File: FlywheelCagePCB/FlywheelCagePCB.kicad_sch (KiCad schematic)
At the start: 10 parts, among them J1 Conn_01x05, J2 Conn_01x05, Q1 SFH320, U1 QRE1113GR, U2 SN74LVC2G14DBV, U3 SPX3819M5-L-3-3

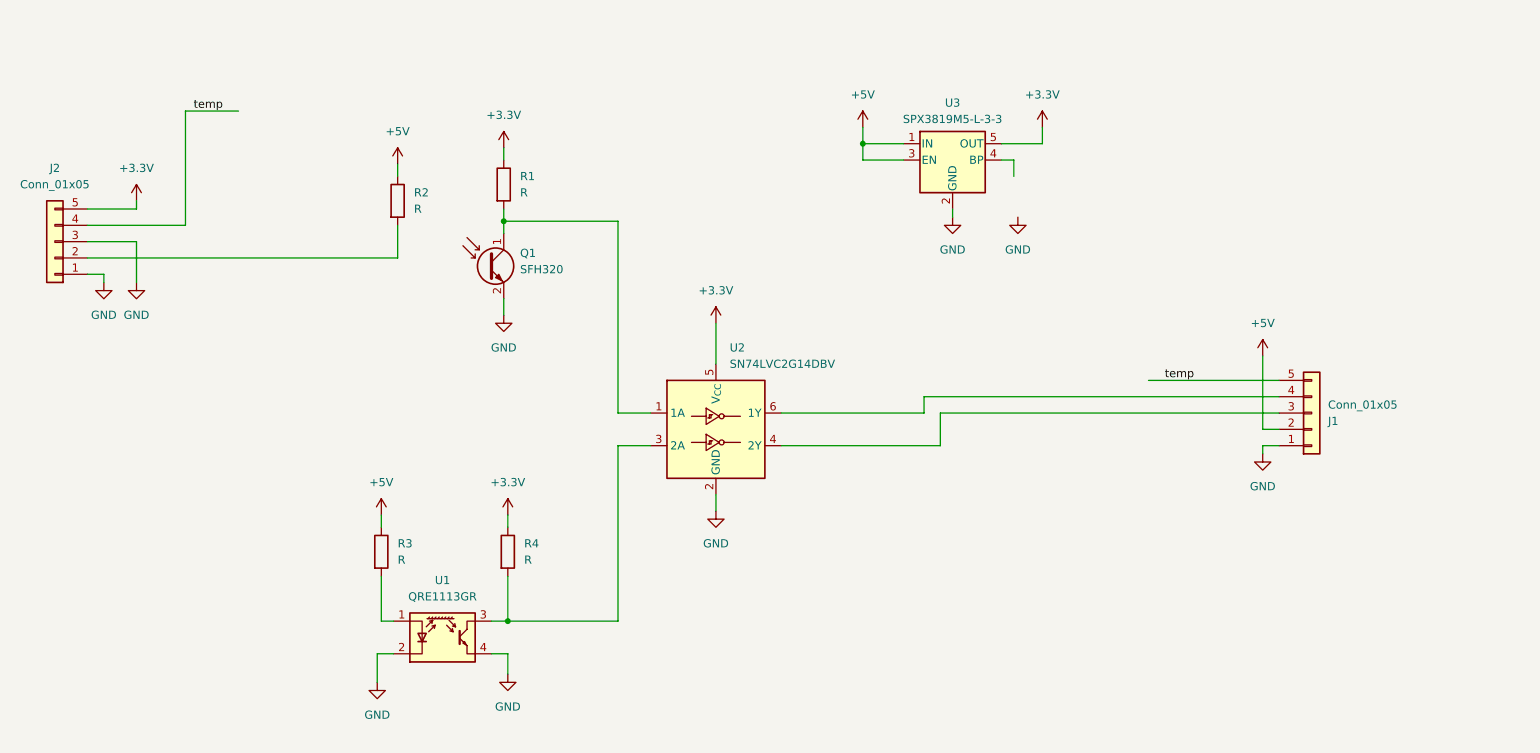
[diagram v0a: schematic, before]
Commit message: added resistors to flywheel pcb
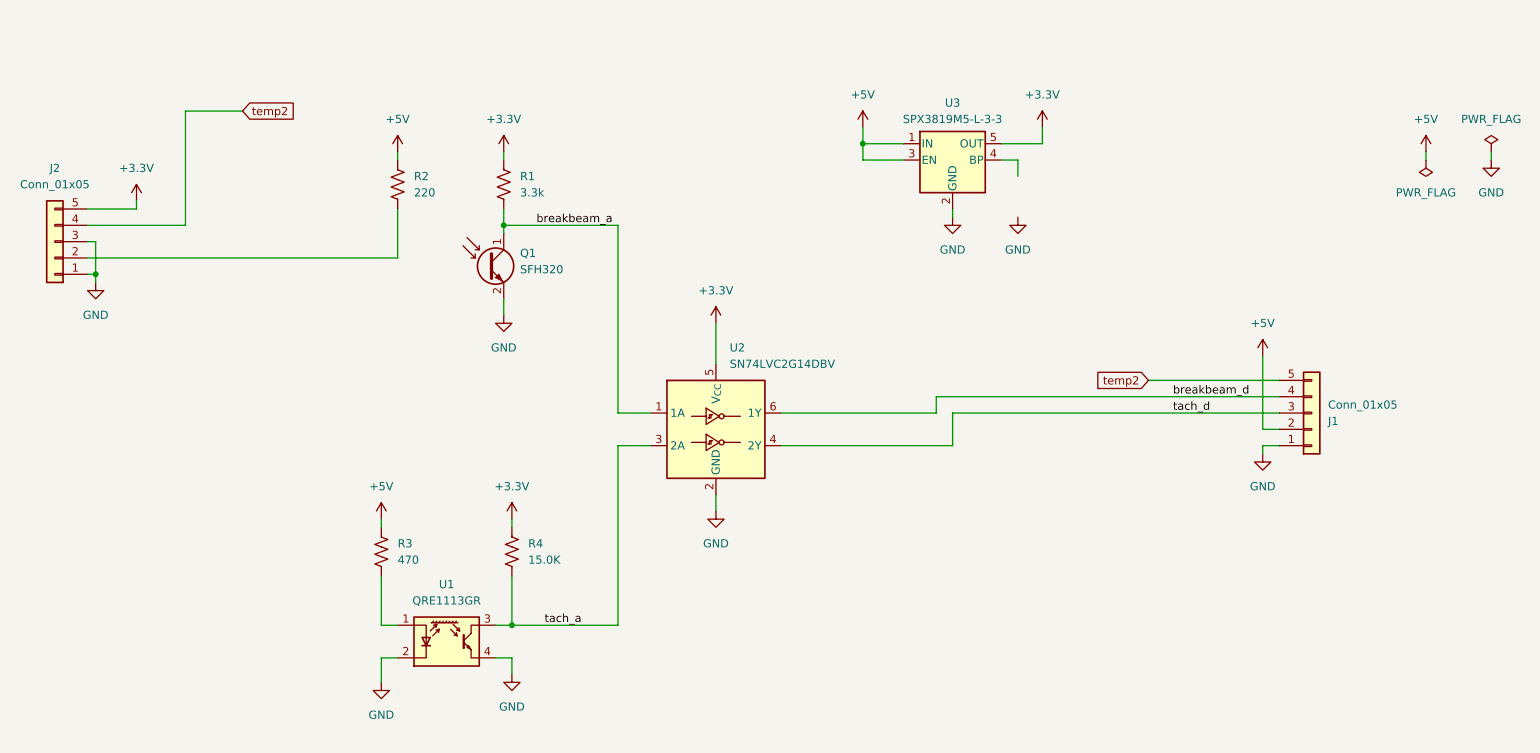
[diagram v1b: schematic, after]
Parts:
- removed R1, R2, R3, R4: R, symbol Device:R
- added R1: 3.3k, Resistor_SMD:R_0603_1608Metric, symbol Passives:R_3.3k_0603
- added R2: 220, Resistor_SMD:R_0603_1608Metric, symbol Passives:R_220_0603
- added R3: 470, Resistor_SMD:R_0603_1608Metric, symbol Passives:R_470_0603
- added R4: 15.0K, Resistor_SMD:R_0603_1608Metric, symbol Passives:R_15.0K_0603
- U2: PartNumber (none) -> 1727-6088-1-ND
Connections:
- net +3.3V: now also R1.1, R4.1
- net +5V: now also R2.1, R3.1
- net breakbeam_a: now reaches Q1.1 (C), U2.1 (1A)
- net breakbeam_a: now also R1.2
- net at U1.1 (A): now also R3.2
- net tach_a: now reaches U1.3, U2.3 (2A)
- net tach_a: now also R4.2
- net at J2.2 (Pin_2): now also R2.2
- net tach_d: now reaches J1.3 (Pin_3), U2.4 (2Y)
- net breakbeam_d: now reaches J1.4 (Pin_4), U2.6 (1Y)
- net temp renamed temp2
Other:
- moved on the sheet: U1

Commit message: moved PCB components a bit
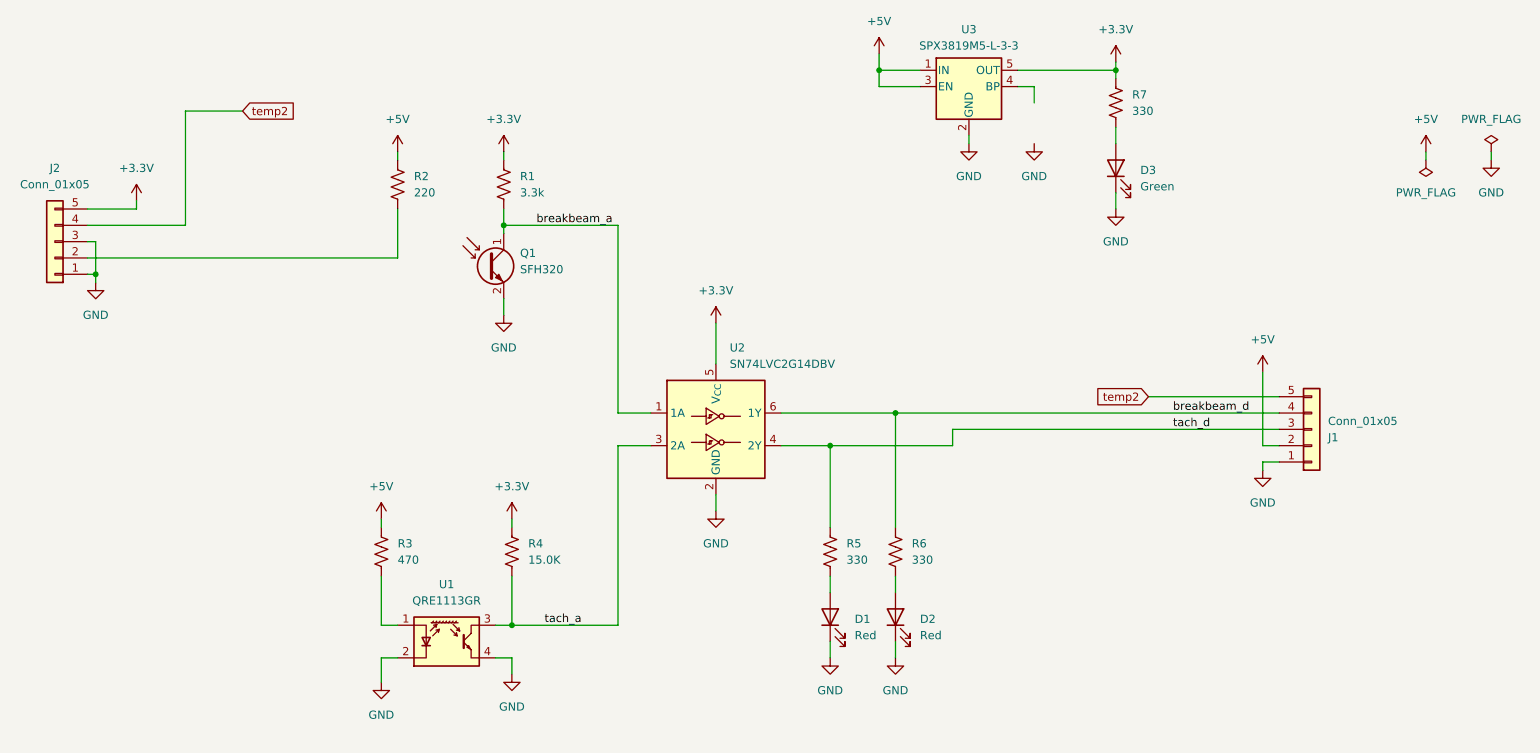
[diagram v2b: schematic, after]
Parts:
- added D1, D2: Red, symbol Passives:LED_RED_0603
- added D3: Green, LED_SMD:LED_0603_1608Metric, symbol Passives:LED_GREEN_0603
- added R5, R6, R7: 330, Resistor_SMD:R_0603_1608Metric, symbol Passives:R_330_0603
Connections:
- net +3.3V: now also R7.1
- net GND: now also D1.1 (K), D2.1 (K), D3.1 (K)
- net breakbeam_d: now also R6.1
- net tach_d: now also R5.1
- new net: D2.2 (A), R6.2
- new net: D1.2 (A), R5.2
- new net: D3.2 (A), R7.2
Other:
- moved on the sheet: J1, U3

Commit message: Added 3d models for JST ZH connectors.  Made 3d Step output
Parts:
- removed Q1: SFH320, LED_SMD:LED_PLCC-2_3.4x3.0mm_KA, symbol Sensor_Optical:SFH320
- added D4: SFH_320-4-Z, McLibrary:PHODET_SFH_320-4-Z, symbol Passives:SFH_320-4-Z
- D1, D2: footprint (none) -> LED_SMD:LED_0603_1608Metric
- J1, J2: footprint Connector_JST:JST_ZH_S5B-ZR-SM4A-TF_1x05-1MP_P1.50mm_Horizontal -> McLibrary:JST_ZH_B5B-ZR_1x05_P1.50mm_Horizontal; symbol Connector_Generic:Conn_01x05 -> Passives:Conn_JST_ZH_S5B_Horizontal_01x05
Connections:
- net GND: now also D4.E
- net breakbeam_a: now also D4.C
- net breakbeam_led_ind: now reaches D2.2 (A), R6.2
- net breakbeam_led: now reaches J2.2 (Pin_2), R2.2
- net tach_led: now reaches R3.2, U1.1 (A)
- net tach_led_ind: now reaches D1.2 (A), R5.2
- net power_led_ind: now reaches D3.2 (A), R7.2
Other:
- moved on the sheet: D1, D2, R3, R5, R6

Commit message: Added caps.  Need to get part numbers
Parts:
- added C1: 0.01uf, Capacitor_SMD:C_0603_1608Metric, symbol Device:C_Small
- added C2: 1uf, Capacitor_SMD:C_0603_1608Metric, symbol Device:C_Small
- added C3: 0.1uf, Capacitor_SMD:C_0603_1608Metric, symbol Device:C_Small
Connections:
- net +3.3V: now also C2.1, C3.1
- net GND: now also C1.2, C2.2, C3.2
- net at U3.4 (BP): now also C1.1
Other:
- moved on the sheet: D3, R7

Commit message: BOM scrubb
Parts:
- removed C1: 0.01uf, Capacitor_SMD:C_0603_1608Metric, symbol Device:C_Small
- added C1: 0.01uf, Capacitor_SMD:C_0603_1608Metric, symbol Passives:C_0.01uf_0603
- C2: symbol Device:C_Small -> Passives:C_1uf_0603; PartNumber (none) -> 399-C0603C105K3RACTUCT-ND
- C3: symbol Device:C_Small -> Passives:C_0.1uf_0603; PartNumber (none) -> 399-C0603C104M5RACTUCT-ND
- D1, D2: PartNumber (none) -> 475-KSEELP41.22-P1R2-58-A8J8-020-R18CT-ND
- D3: PartNumber (none) -> 475-KGEELP41.22-PHRH-35-A8J8-20-R18CT-ND
- D4: PartNumber (none) -> 475-SFH320-4-ZCT-ND
- J1, J2: value Conn_01x05 -> JST_ZH_S5B; PartNumber (none) -> 455-S5B-ZR-ND
- U1: symbol Sensor_Proximity:QRE1113GR -> Passives:QRE1113GR; PartNumber (none) -> QRE1113GRCT-ND
- U2: symbol 74xGxx:SN74LVC2G14DBV -> Passives:SN74LVC2G14DBV
- U3: symbol Regulator_Linear:SPX3819M5-L-3-3 -> Passives:SPX3819M5-L-3-3; PartNumber (none) -> 1016-1873-1-ND
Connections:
- net GND: now also C1.2
- net at U3.4 (BP): now also C1.1
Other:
- moved on the sheet: C2
